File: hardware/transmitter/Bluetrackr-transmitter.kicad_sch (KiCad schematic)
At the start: 43 parts, among them J1 USB_C_Receptacle_USB2.0, J2 Programming_Connector, J3 Battery_Connector, Q1 CJ2333, SW1 SW_Pair, U1 MIC5205-2.5YM5, U2 MCP73831-2-OT, U3 STM32F030R8Tx, U4 DL-24N-2.4G, U5 LSM9DS1

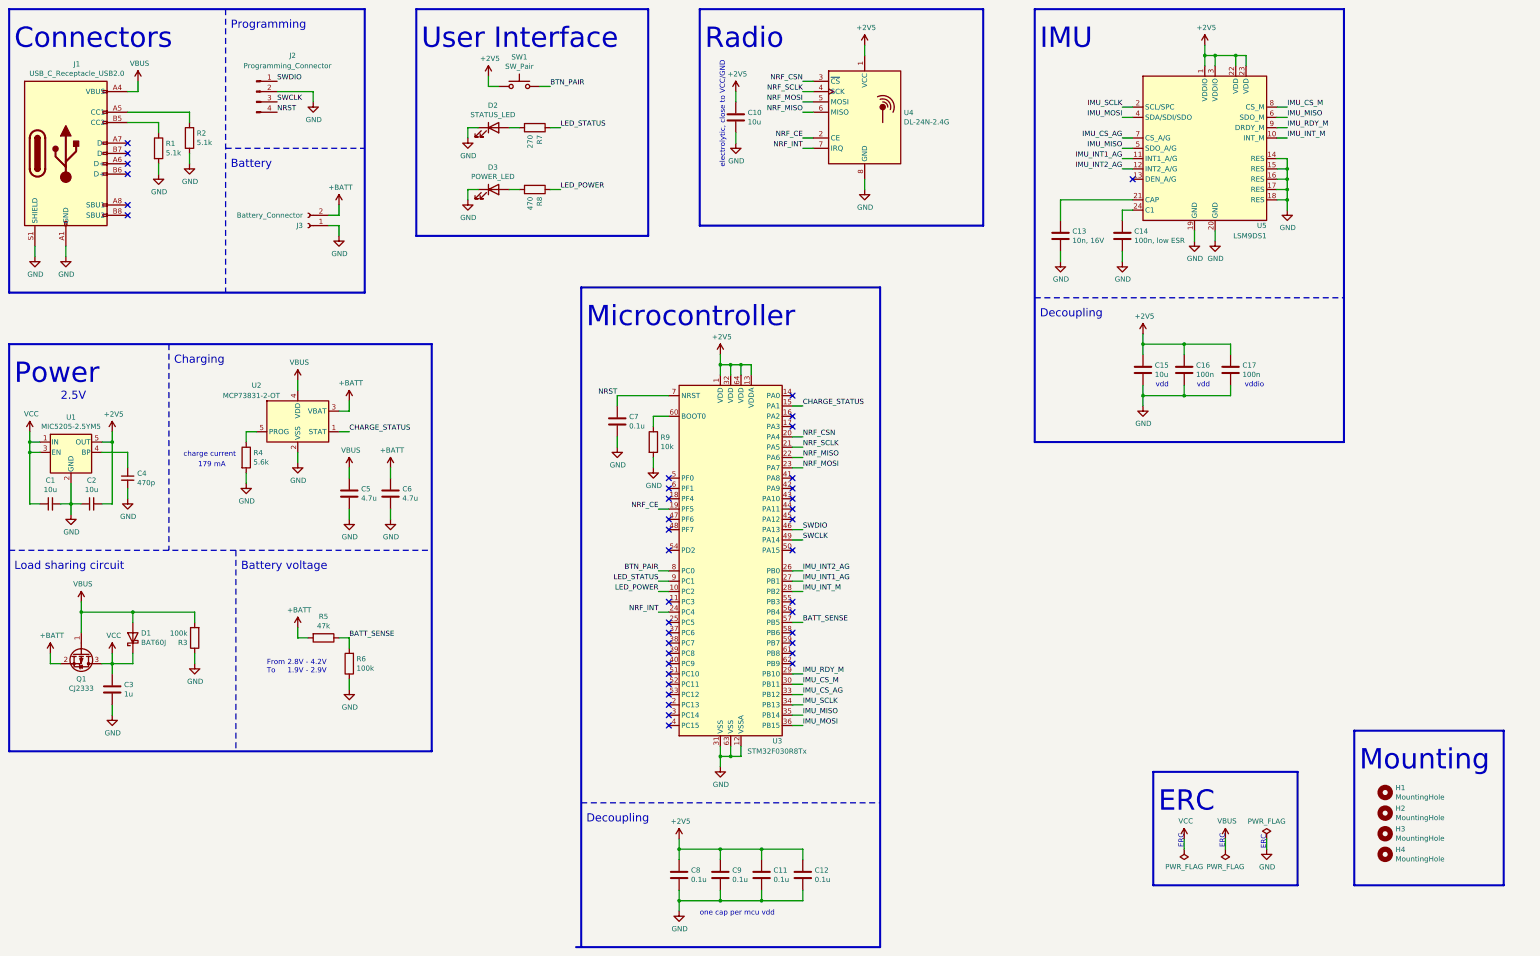
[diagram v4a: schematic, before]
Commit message: Change MCU to STM32F072C8T6 for USB
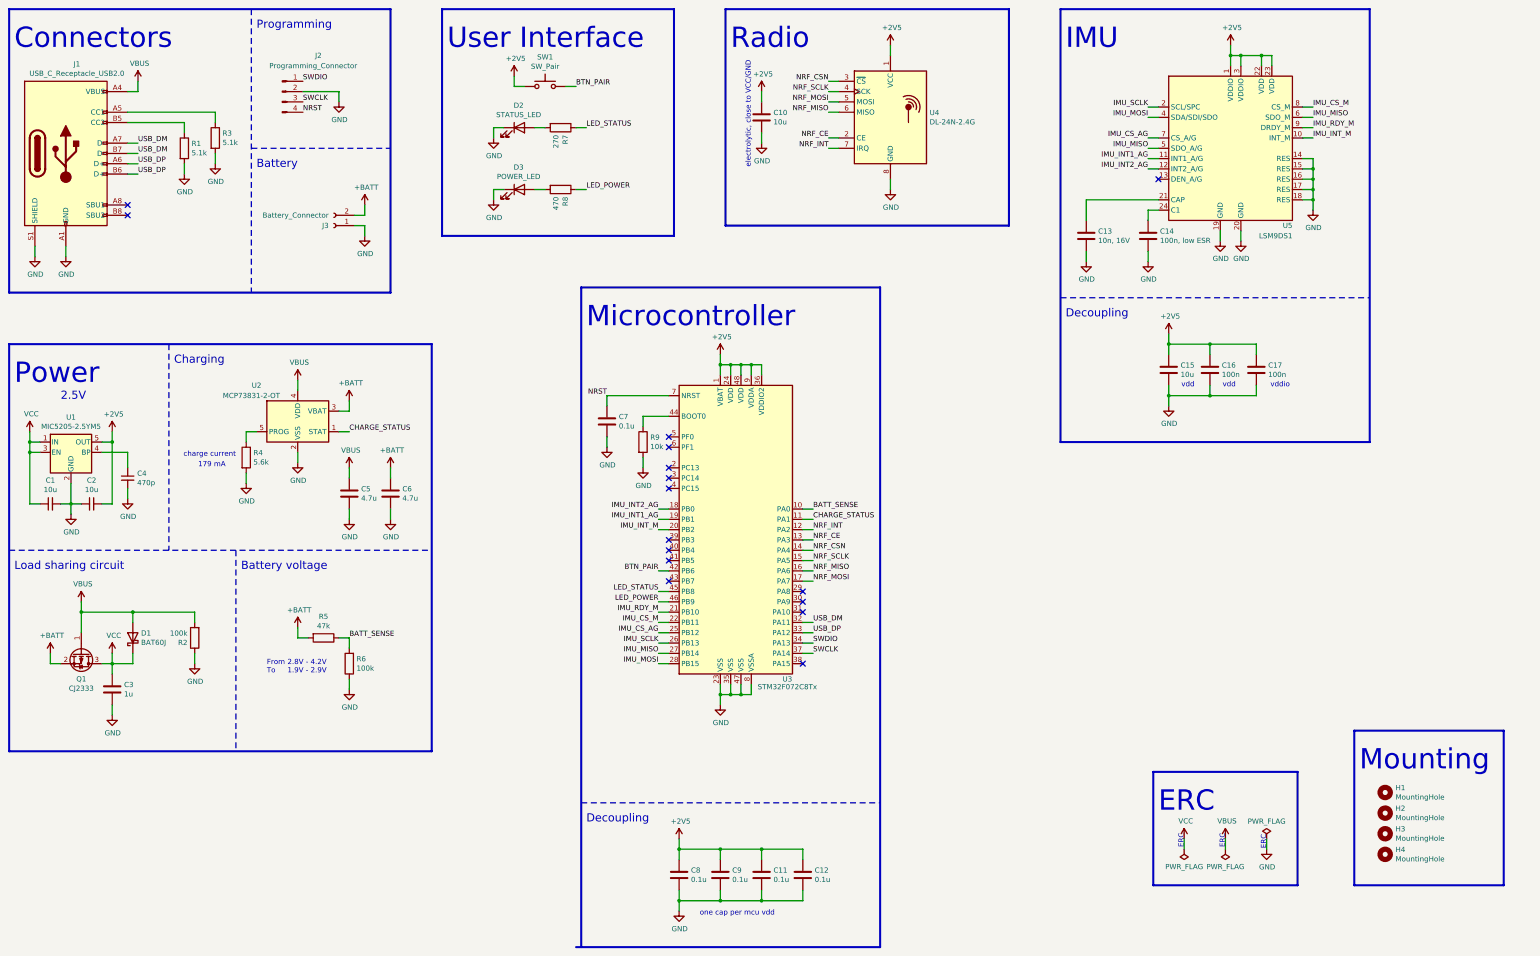
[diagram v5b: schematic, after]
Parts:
- removed U3: STM32F030R8Tx, Package_QFP:LQFP-64_10x10mm_P0.5mm, symbol MCU_ST_STM32F0:STM32F030R8Tx
- added U3: STM32F072C8Tx, Package_QFP:LQFP-48_7x7mm_P0.5mm, symbol MCU_ST_STM32F0:STM32F072C8Tx
- renumbered R3 to R2, R2 to R3
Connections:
- net +2V5: now also U3.1 (VBAT), U3.24 (VDD), U3.36 (VDDIO2), U3.48 (VDD), U3.9 (VDDA)
- net BATT_SENSE: now also U3.10 (PA0)
- net BTN_PAIR: now also U3.42 (PB6)
- net CHARGE_STATUS: now also U3.11 (PA1)
- net GND: now also U3.23 (VSS), U3.35 (VSS), U3.47 (VSS), U3.8 (VSSA)
- net IMU_CS_AG: now also U3.25 (PB12)
- net IMU_CS_M: now also U3.22 (PB11)
- net IMU_INT1_AG: now also U3.19 (PB1)
- net IMU_INT2_AG: now also U3.18 (PB0)
- net IMU_INT_M: now also U3.20 (PB2)
- net IMU_MISO: now also U3.27 (PB14)
- net IMU_MOSI: now also U3.28 (PB15)
- net IMU_RDY_M: now also U3.21 (PB10)
- net IMU_SCLK: now also U3.26 (PB13)
- net LED_POWER: now also U3.46 (PB9)
- net LED_STATUS: now also U3.45 (PB8)
- net NRF_CE: now also U3.13 (PA3)
- net NRF_CSN: now also U3.14 (PA4)
- net NRF_INT: now also U3.12 (PA2)
- net NRF_MISO: now also U3.16 (PA6)
- net NRF_MOSI: now also U3.17 (PA7)
- net NRF_SCLK: now also U3.15 (PA5)
- net NRST: now also U3.7 (NRST)
- net SWCLK: now also U3.37 (PA14)
- net SWDIO: now also U3.34 (PA13)
- net at R9.1: now also U3.44 (BOOT0)
- net USB_DP: now reaches J1.A6 (D+)
- net USB_DP: now also J1.B6 (D+), U3.33 (PA12)
- net USB_DM: now reaches J1.A7 (D-)
- net USB_DM: now also J1.B7 (D-), U3.32 (PA11)
- no-connect marks 40 -> 16
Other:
- moved on the sheet: C10, C13, C14, C15, C16, C17, C7, D2, D3, J2, J3, R1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

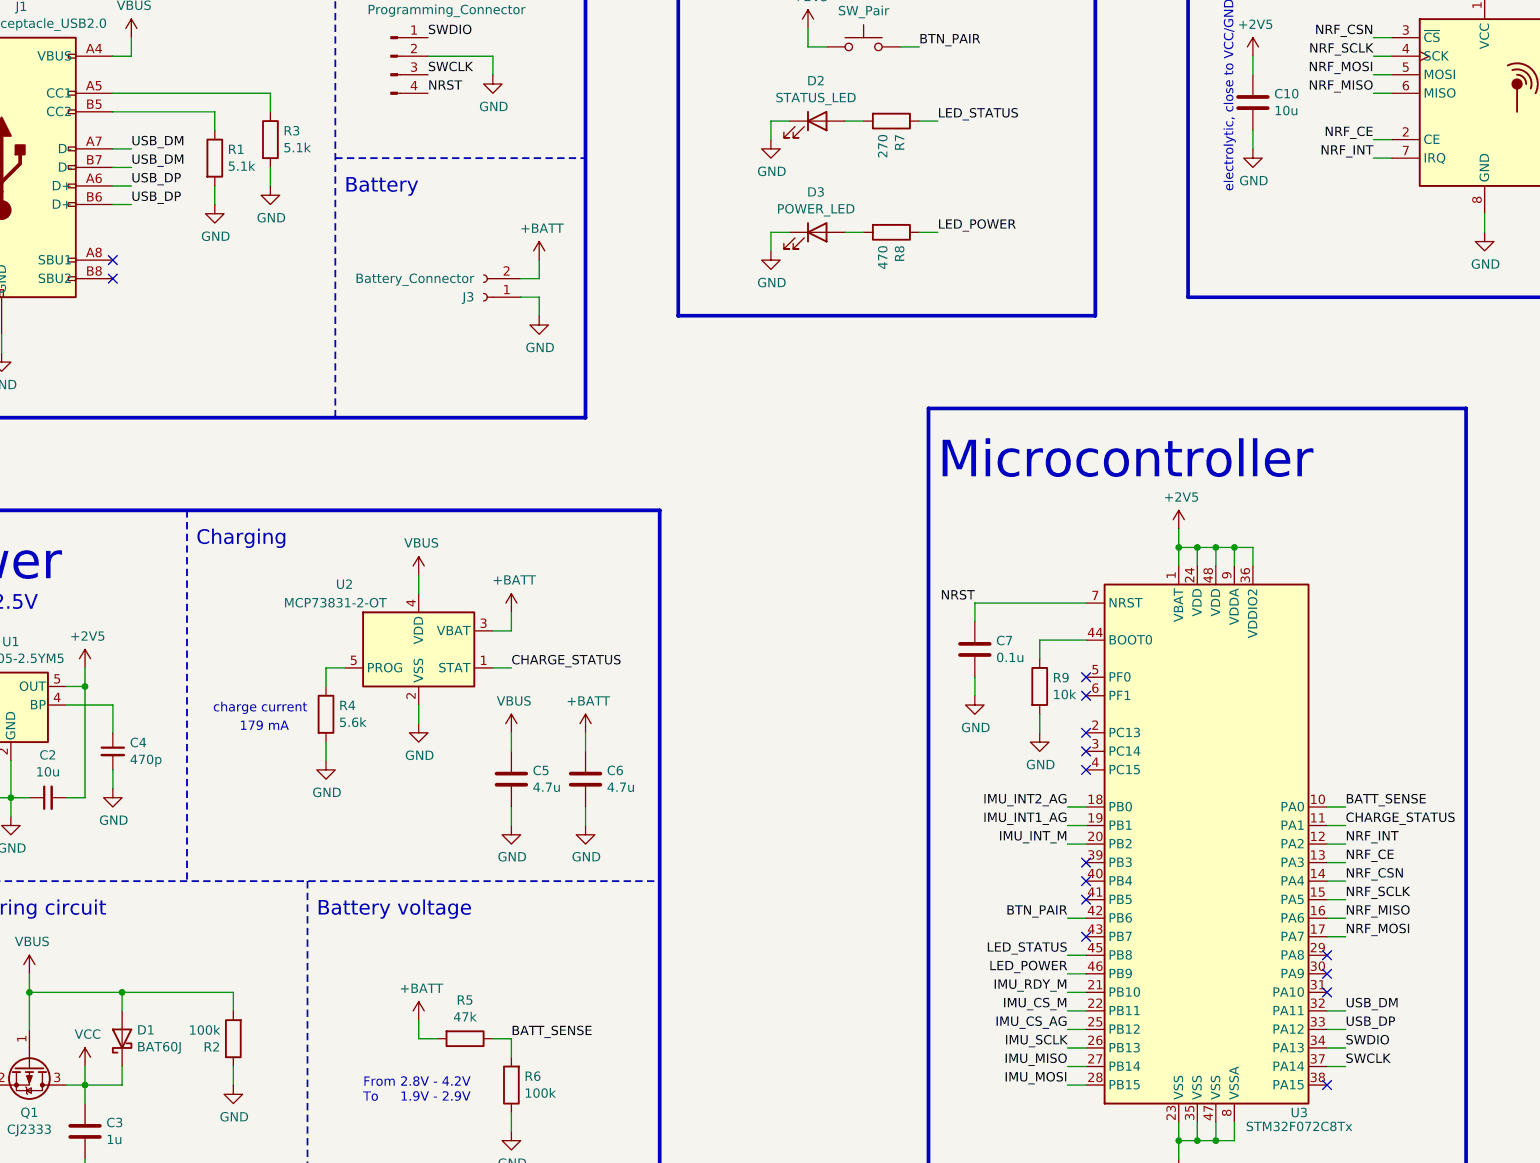
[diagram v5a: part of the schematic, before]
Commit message: Place LEDs
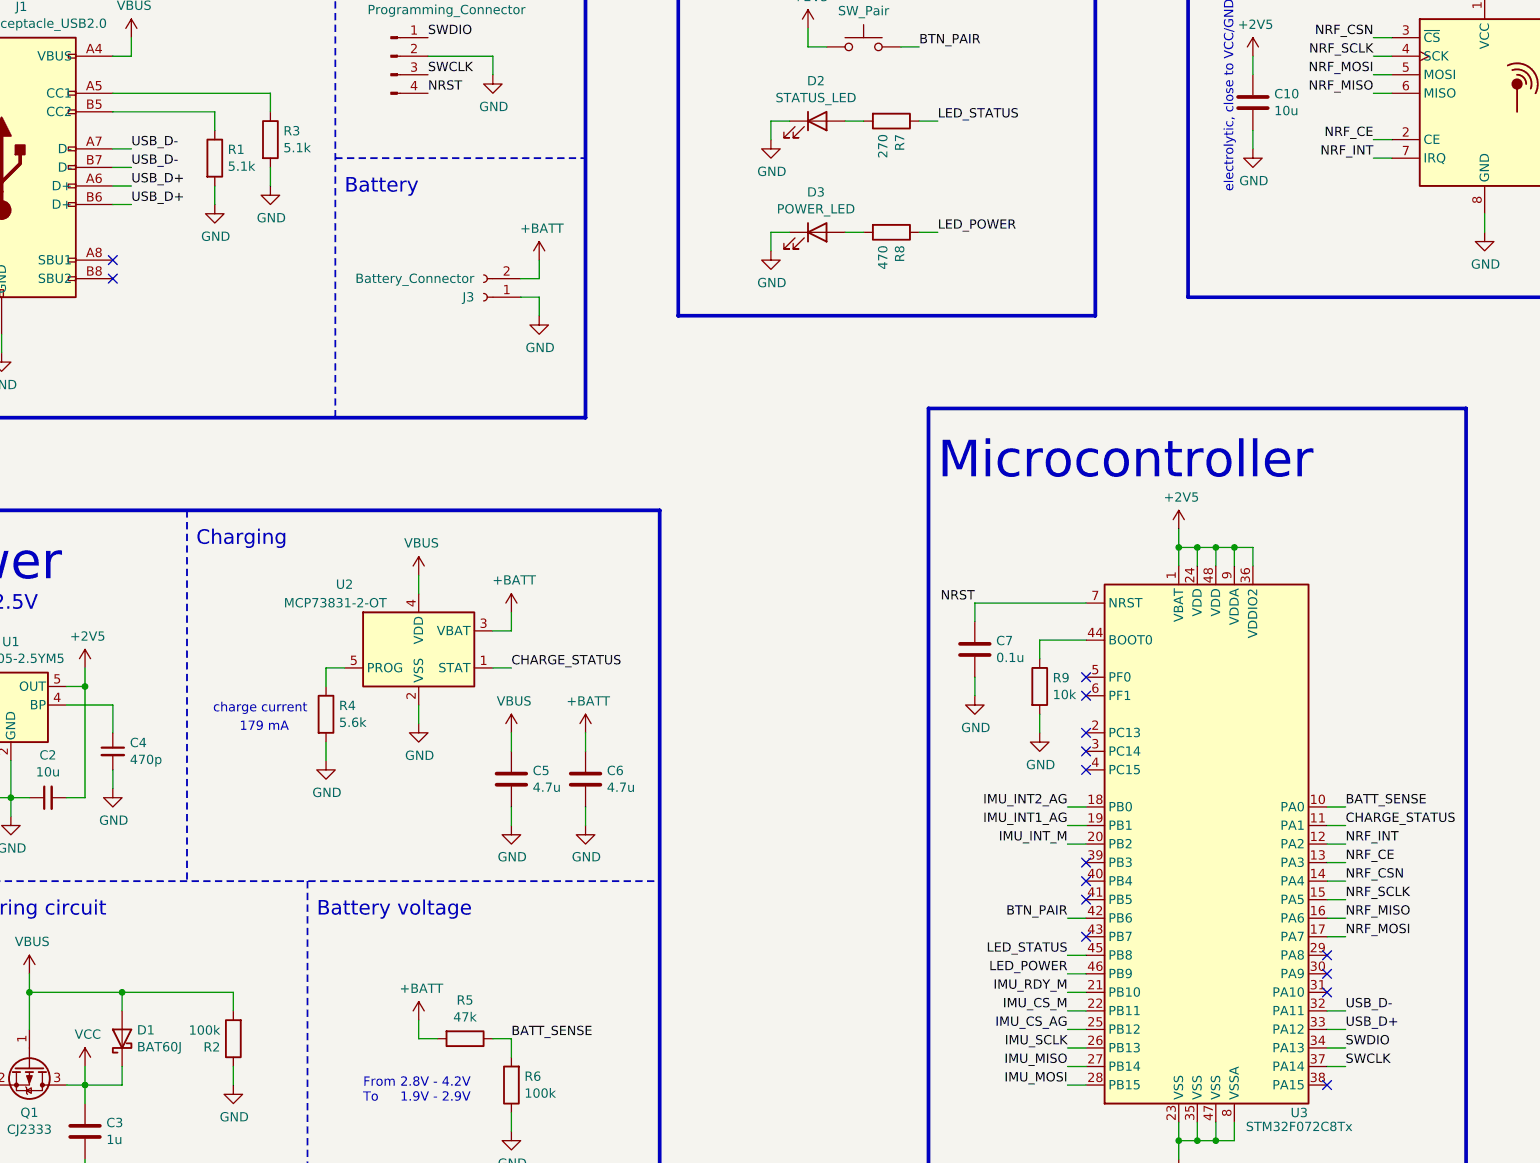
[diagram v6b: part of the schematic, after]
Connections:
- net USB_DM renamed USB_D-
- net USB_DP renamed USB_D+
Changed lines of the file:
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@@
     (effects (font (size 5 5)) (justify left bottom))
   )
-  (label "USB_DM" (at 57.15 58.42 0)
+  (label "USB_D-" (at 57.15 58.42 0)
     (effects (font (size 1.27 1.27)) (justify left bottom))
   )
-  (label "USB_DM" (at 57.15 60.96 0)
+  (label "USB_D-" (at 57.15 60.96 0)
     (effects (font (size 1.27 1.27)) (justify left bottom))
   )
-  (label "USB_DP" (at 57.15 63.5 0)
+  (label "USB_D+" (at 57.15 63.5 0)
     (effects (font (size 1.27 1.27)) (justify left bottom))
   )
-  (label "USB_DP" (at 57.15 66.04 0)
+  (label "USB_D+" (at 57.15 66.04 0)
     (effects (font (size 1.27 1.27)) (justify left bottom))
   )
@@
     (effects (font (size 1.27 1.27)) (justify left bottom))
   )
-  (label "USB_DM" (at 223.52 176.53 0)
+  (label "USB_D-" (at 223.52 176.53 0)
     (effects (font (size 1.27 1.27)) (justify left bottom))
   )
-  (label "USB_DP" (at 223.52 179.07 0)
+  (label "USB_D+" (at 223.52 179.07 0)
     (effects (font (size 1.27 1.27)) (justify left bottom))
   )

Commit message: Change connectors to ZH SMD versions
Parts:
- J2: footprint Connector_JST:JST_XH_B4B-XH-A_1x04_P2.50mm_Vertical -> User_Connector_JST:JST_B4B-ZR-SM4-TF
- J3: footprint Connector_JST:JST_XH_S2B-XH-A_1x02_P2.50mm_Horizontal -> User_Connector_JST:JST_S2B-ZR-SM4A-TF
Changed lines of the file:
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@@
       (effects (font (size 1.27 1.27)) (justify left))
     )
-    (property "Footprint" "Connector_JST:JST_XH_S2B-XH-A_1x02_P2.50mm_Horizontal" (id 2) (at 105.41 78.74 0)
+    (property "Footprint" "User_Connector_JST:JST_S2B-ZR-SM4A-TF" (id 2) (at 105.41 78.74 0)
       (effects (font (size 1.27 1.27)) hide)
     )
@@
     (property "Reference" "J2" (id 0) (at 101.6 36.83 0))
     (property "Value" "Programming_Connector" (id 1) (at 100.33 39.37 0))
-    (property "Footprint" "Connector_JST:JST_XH_B4B-XH-A_1x04_P2.50mm_Vertical" (id 2) (at 92.71 45.72 0)
-      (effects (font (size 1.27 1.27)) hide)
-    )
+    (property "Footprint" "User_Connector_JST:JST_B4B-ZR-SM4-TF" (id 2) (at 92.71 45.72 0)
+      (effects (font (size 1.27 1.27)) hide)
+    )
